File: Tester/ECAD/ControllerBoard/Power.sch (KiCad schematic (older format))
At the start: 10 parts, among them U6 TPS2041B, U7 TLV70033_SOT23-5, U8 TLV70033_SOT23-5

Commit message: Progressed circuit layout.
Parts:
- removed U6: TPS2041B, Package_TO_SOT_SMD:SOT-23-5, symbol Power_Management:TPS2041B
- added C10: 0.1uC, Capacitor_SMD:C_0805_2012Metric_Pad1.15x1.40mm_HandSolder, symbol Device:C
- added C11: 150uCP, symbol Device:CP
- added R23: 10kR, Resistor_SMD:R_0805_2012Metric_Pad1.15x1.40mm_HandSolder, symbol Device:R
- added U6: TPS2046B, Package_SO:SOIC-8_3.9x4.9mm_P1.27mm, symbol Power_Management_Custom:TPS2046B
- R6: value R -> 10kR
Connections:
- net labels added: LOAD_OVERCURRENT_DIGITAL_LOGIC, LOAD_OVERCURRENT_MOTOR, V3_3, ~POWER_SWITCH_ANALOGUE_LOADS, ~POWER_SWITCH_DIGITAL_LOGIC
- net labels removed: V3_3_SENS, ~POWER_SWITCH
- wire segments 49 -> 71
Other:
- moved on the sheet: C31, C32, C8, C9, R6, U8

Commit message: Update Power.sch
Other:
- moved on the sheet: C8
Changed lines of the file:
@@
 L Device:C C8
 U 1 1 5E61FCAC
-P 7000 2250
-F 0 "C8" H 7115 2296 50  0000 L CNN
-F 1 "0.1uC" H 7115 2205 50  0000 L CNN
-F 2 "Capacitor_SMD:C_0805_2012Metric_Pad1.15x1.40mm_HandSolder" H 7038 2100 50  0001 C CNN
-F 3 "~" H 7000 2250 50  0001 C CNN
-F 4 "" H 7000 2250 50  0001 C CNN "Manufacturer Part Number"
-	1    7000 2250
+P 6700 3150
+F 0 "C8" H 6815 3196 50  0000 L CNN
+F 1 "0.1uC" H 6815 3105 50  0000 L CNN
+F 2 "Capacitor_SMD:C_0805_2012Metric_Pad1.15x1.40mm_HandSolder" H 6738 3000 50  0001 C CNN
+F 3 "~" H 6700 3150 50  0001 C CNN
+F 4 "" H 6700 3150 50  0001 C CNN "Manufacturer Part Number"
+	1    6700 3150
 	1    0    0    -1
 $EndComp
-Wire Wire Line
-	6700 2000 7000 2000
-Connection ~ 6700 2000
 Connection ~ 6000 3650
 $Comp
@@
 Text HLabel 4750 2700 0    50   Output ~ 0
 LOAD_OVERCURRENT_DIGITAL_LOGIC
-Wire Wire Line
-	7000 2100 7000 2000
-Wire Wire Line
-	7000 2400 7000 3650
-Wire Wire Line
-	7000 3650 6000 3650
 Connection ~ 7200 2800
 Wire Wire Line
 	7200 3300 7200 3650
-Wire Wire Line
-	7200 3650 7000 3650
-Connection ~ 7000 3650
 $Comp
 L Device:C C10
@@
 Wire Wire Line
 	7750 2800 9100 2800
+Connection ~ 6700 2600
+Connection ~ 6700 3650
+Wire Wire Line
+	6700 3650 6000 3650
+Wire Wire Line
+	6700 3650 7200 3650
+Wire Wire Line
+	6700 3000 6700 2600
+Wire Wire Line
+	6700 3300 6700 3650
 $EndSCHEMATC

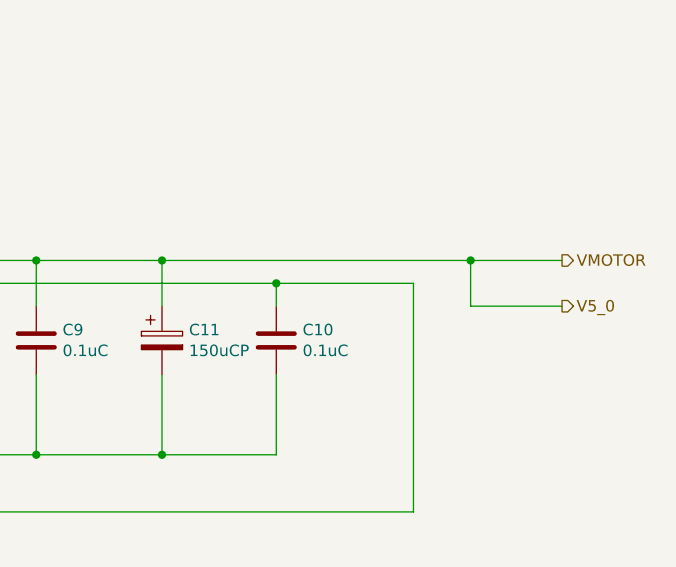
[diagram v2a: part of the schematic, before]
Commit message: Progressed circuit layout.
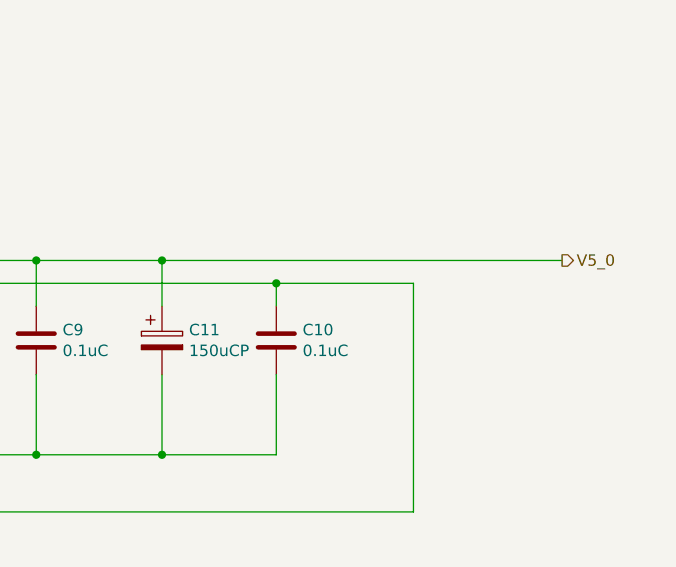
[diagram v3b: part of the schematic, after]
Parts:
- C10, C8, C9: Manufacturer Part Number (none) -> CC0805ZRY5V8BB104
- C11: footprint (none) -> Capacitor_Tantalum_SMD:CP_EIA-7343-31_Kemet-D_Pad2.25x2.55mm_HandSolder
- R23, R6: Manufacturer Part Number (none) -> RC0805FR-0710KL
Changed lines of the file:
@@
 Text HLabel 850  7500 0    50   Input ~ 0
 GND
-Text HLabel 9500 2800 2    50   Output ~ 0
-VMOTOR
 Text HLabel 9400 1050 2    50   Output ~ 0
 V3_3_MCU
-Text HLabel 9500 3000 2    50   Output ~ 0
+Text HLabel 9500 2800 2    50   Output ~ 0
 V5_0
 $Comp
@@
 F 2 "Capacitor_SMD:C_0805_2012Metric_Pad1.15x1.40mm_HandSolder" H 6738 3000 50  0001 C CNN
 F 3 "~" H 6700 3150 50  0001 C CNN
-F 4 "" H 6700 3150 50  0001 C CNN "Manufacturer Part Number"
+F 4 "CC0805ZRY5V8BB104" H 6700 3150 50  0001 C CNN "Manufacturer Part Number"
 	1    6700 3150
 	1    0    0    -1
@@
 F 2 "Capacitor_SMD:C_0805_2012Metric_Pad1.15x1.40mm_HandSolder" H 7238 3000 50  0001 C CNN
 F 3 "~" H 7200 3150 50  0001 C CNN
-F 4 "" H 7200 3150 50  0001 C CNN "Manufacturer Part Number"
+F 4 "CC0805ZRY5V8BB104" H 7200 3150 50  0001 C CNN "Manufacturer Part Number"
 	1    7200 3150
 	1    0    0    -1
@@
 F 2 "Resistor_SMD:R_0805_2012Metric_Pad1.15x1.40mm_HandSolder" V 4780 2300 50  0001 C CNN
 F 3 "~" H 4850 2300 50  0001 C CNN
+F 4 "RC0805FR-0710KL" H 4850 2300 50  0001 C CNN "Manufacturer Part Number"
 	1    4850 2300
 	1    0    0    -1
@@
 Wire Wire Line
 	4950 3900 4950 4350
-Wire Wire Line
-	9500 3000 9100 3000
-Wire Wire Line
-	9100 3000 9100 2800
-Connection ~ 9100 2800
-Wire Wire Line
-	9100 2800 9500 2800
 Text HLabel 5500 3100 0    50   Input ~ 0
 ~POWER_SWITCH_DIGITAL_LOGIC
@@
 F 2 "Resistor_SMD:R_0805_2012Metric_Pad1.15x1.40mm_HandSolder" V 5130 2300 50  0001 C CNN
 F 3 "~" H 5200 2300 50  0001 C CNN
+F 4 "RC0805FR-0710KL" H 5200 2300 50  0001 C CNN "Manufacturer Part Number"
 	1    5200 2300
 	1    0    0    -1
@@
 F 2 "Capacitor_SMD:C_0805_2012Metric_Pad1.15x1.40mm_HandSolder" H 8288 3000 50  0001 C CNN
 F 3 "~" H 8250 3150 50  0001 C CNN
-F 4 "" H 8250 3150 50  0001 C CNN "Manufacturer Part Number"
+F 4 "CC0805ZRY5V8BB104" H 8250 3150 50  0001 C CNN "Manufacturer Part Number"
 	1    8250 3150
 	1    0    0    -1
@@
 F 0 "C11" H 7868 3196 50  0000 L CNN
 F 1 "150uCP" H 7868 3105 50  0000 L CNN
-F 2 "" H 7788 3000 50  0001 C CNN
+F 2 "Capacitor_Tantalum_SMD:CP_EIA-7343-31_Kemet-D_Pad2.25x2.55mm_HandSolder" H 7788 3000 50  0001 C CNN
 F 3 "~" H 7750 3150 50  0001 C CNN
 F 4 "T495D157K010ATE100" H 7750 3150 50  0001 C CNN "Manufacturer Part Number"
@@
 	7750 3000 7750 2800
 Connection ~ 7750 2800
-Wire Wire Line
-	7750 2800 9100 2800
 Connection ~ 6700 2600
 Connection ~ 6700 3650
@@
 Wire Wire Line
 	6700 3300 6700 3650
+Wire Wire Line
+	7750 2800 9500 2800
 $EndSCHEMATC

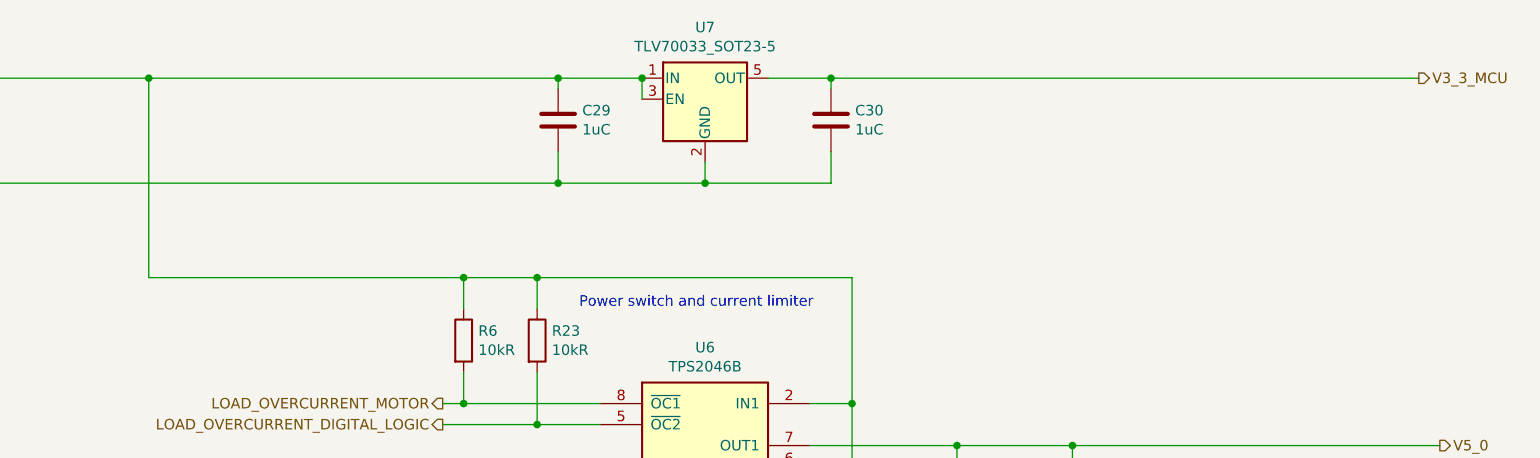
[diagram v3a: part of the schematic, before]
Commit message: Progressed circuit layout.
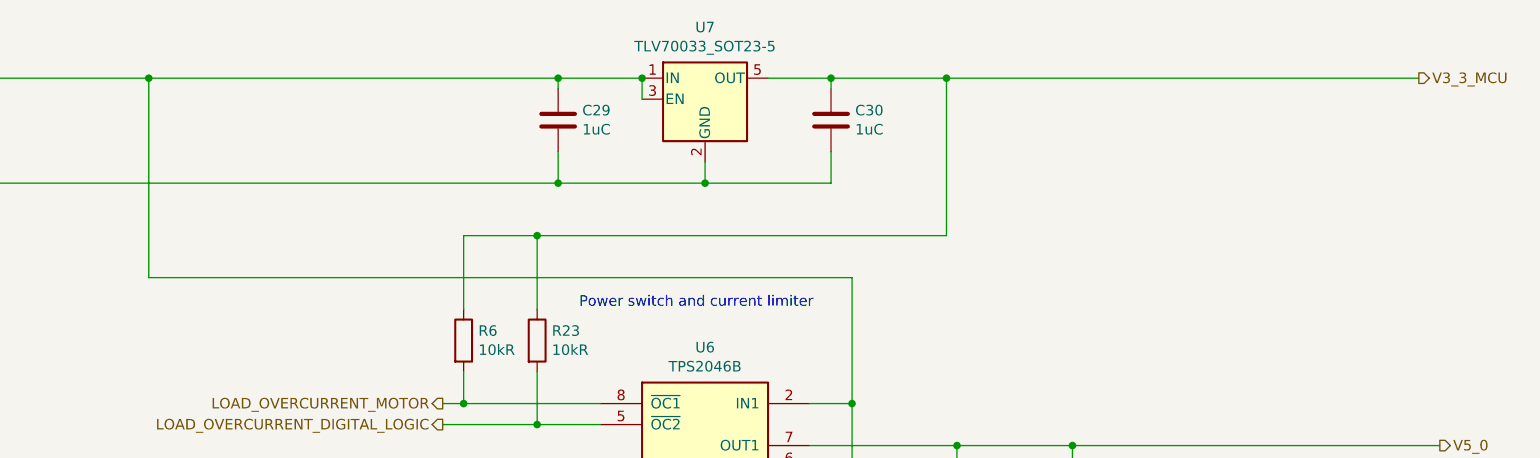
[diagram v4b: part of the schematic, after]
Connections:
- net V3_3_MCU: now also R23.1, R6.1
- net V5_USB: no longer R23.1, R6.1
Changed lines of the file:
@@
 Connection ~ 6600 1050
 Wire Wire Line
-	6600 1050 9400 1050
+	6600 1050 7150 1050
 Wire Wire Line
 	6600 1400 6600 1550
@@
 	6500 2600 6700 2600
 Wire Wire Line
-	6700 2000 5200 2000
-Wire Wire Line
 	3350 2000 3350 1050
 Connection ~ 3350 1050
@@
 Wire Wire Line
 	4850 2600 4850 2450
-Wire Wire Line
-	4850 2150 4850 2000
 Text Notes 5400 2150 0    50   ~ 0
 Power switch and current limiter
@@
 	5200 2700 5200 2450
 Wire Wire Line
-	5200 2150 5200 2000
-Connection ~ 5200 2000
-Wire Wire Line
 	5200 2700 4750 2700
 Connection ~ 5200 2700
@@
 	7750 3650 7200 3650
 Connection ~ 7200 3650
-Connection ~ 4850 2000
-Wire Wire Line
-	4850 2000 3350 2000
-Wire Wire Line
-	4850 2000 5200 2000
 Connection ~ 4850 2600
 Wire Wire Line
@@
 Wire Wire Line
 	7750 2800 9500 2800
+Wire Wire Line
+	3350 2000 6700 2000
+Wire Wire Line
+	7150 1050 7150 1800
+Wire Wire Line
+	7150 1800 5200 1800
+Wire Wire Line
+	4850 1800 4850 2150
+Connection ~ 7150 1050
+Wire Wire Line
+	7150 1050 9400 1050
+Wire Wire Line
+	5200 2150 5200 1800
+Connection ~ 5200 1800
+Wire Wire Line
+	5200 1800 4850 1800
 $EndSCHEMATC

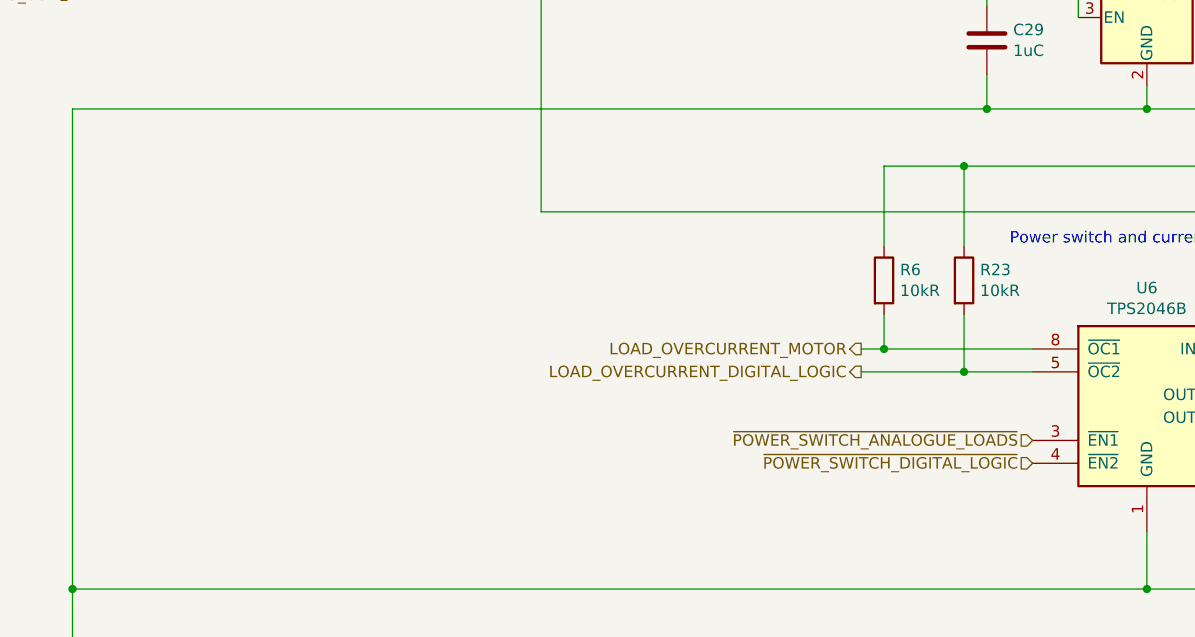
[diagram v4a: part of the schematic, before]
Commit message: Progressed circuit layout.
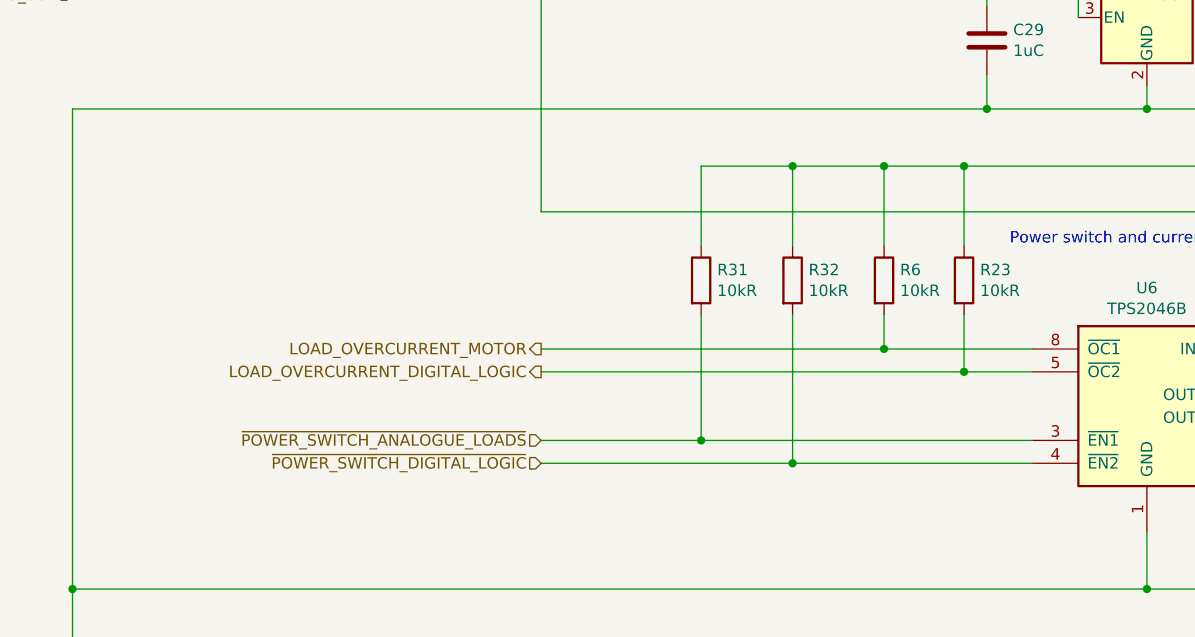
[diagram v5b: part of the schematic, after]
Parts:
- added R31, R32: 10kR, Resistor_SMD:R_0805_2012Metric_Pad1.15x1.40mm_HandSolder, symbol Device:R
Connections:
- net V3_3_MCU: now also R31.1, R32.1
- net ~POWER_SWITCH_ANALOGUE_LOADS: now also R31.2
- net ~POWER_SWITCH_DIGITAL_LOGIC: now also R32.2
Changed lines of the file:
@@
 Wire Wire Line
 	7200 2800 7200 3000
-Text HLabel 5500 3000 0    50   Input ~ 0
+Text HLabel 3350 3000 0    50   Input ~ 0
 ~POWER_SWITCH_ANALOGUE_LOADS
 $Comp
@@
 Text Notes 5400 2150 0    50   ~ 0
 Power switch and current limiter
-Text HLabel 4750 2600 0    50   Output ~ 0
+Text HLabel 3350 2600 0    50   Output ~ 0
 LOAD_OVERCURRENT_MOTOR
 Wire Wire Line
@@
 Wire Wire Line
 	4950 3900 4950 4350
-Text HLabel 5500 3100 0    50   Input ~ 0
+Text HLabel 3350 3100 0    50   Input ~ 0
 ~POWER_SWITCH_DIGITAL_LOGIC
 $Comp
@@
 Wire Wire Line
 	5200 2700 5200 2450
-Wire Wire Line
-	5200 2700 4750 2700
 Connection ~ 5200 2700
-Text HLabel 4750 2700 0    50   Output ~ 0
+Text HLabel 3350 2700 0    50   Output ~ 0
 LOAD_OVERCURRENT_DIGITAL_LOGIC
 Connection ~ 7200 2800
@@
 Connection ~ 4850 2600
 Wire Wire Line
-	4850 2600 4750 2600
-Wire Wire Line
 	4850 2600 5500 2600
 $Comp
@@
 Wire Wire Line
 	5200 1800 4850 1800
+$Comp
+L Device:R R31
+U 1 1 5E6464A0
+P 4050 2300
+F 0 "R31" H 4120 2346 50  0000 L CNN
+F 1 "10kR" H 4120 2255 50  0000 L CNN
+F 2 "Resistor_SMD:R_0805_2012Metric_Pad1.15x1.40mm_HandSolder" V 3980 2300 50  0001 C CNN
+F 3 "~" H 4050 2300 50  0001 C CNN
+F 4 "RC0805FR-0710KL" H 4050 2300 50  0001 C CNN "Manufacturer Part Number"
+	1    4050 2300
+	1    0    0    -1
+$EndComp
+$Comp
+L Device:R R32
+U 1 1 5E64669F
+P 4450 2300
+F 0 "R32" H 4520 2346 50  0000 L CNN
+F 1 "10kR" H 4520 2255 50  0000 L CNN
+F 2 "Resistor_SMD:R_0805_2012Metric_Pad1.15x1.40mm_HandSolder" V 4380 2300 50  0001 C CNN
+F 3 "~" H 4450 2300 50  0001 C CNN
+F 4 "RC0805FR-0710KL" H 4450 2300 50  0001 C CNN "Manufacturer Part Number"
+	1    4450 2300
+	1    0    0    -1
+$EndComp
+Wire Wire Line
+	3350 2600 4850 2600
+Wire Wire Line
+	3350 2700 5200 2700
+Wire Wire Line
+	5500 3000 4050 3000
+Wire Wire Line
+	5500 3100 4450 3100
+Wire Wire Line
+	4450 2450 4450 3100
+Connection ~ 4450 3100
+Wire Wire Line
+	4450 3100 3350 3100
+Wire Wire Line
+	4050 2450 4050 3000
+Connection ~ 4050 3000
+Wire Wire Line
+	4050 3000 3350 3000
+Wire Wire Line
+	4050 2150 4050 1800
+Wire Wire Line
+	4050 1800 4450 1800
+Connection ~ 4850 1800
+Wire Wire Line
+	4450 2150 4450 1800
+Connection ~ 4450 1800
+Wire Wire Line
+	4450 1800 4850 1800
 $EndSCHEMATC

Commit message: Progressed PCB layout.
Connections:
- net OUT2: now reaches C10.1, C31.1, U6.6 (OUT2), U8.1 (IN), U8.3 (EN)
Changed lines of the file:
@@
 Wire Wire Line
 	4450 1800 4850 1800
+Text Label 6900 3900 0    50   ~ 0
+OUT2
 $EndSCHEMATC

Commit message: Progressed circuit updates.
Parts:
- removed C31, C32: 1uC, Capacitor_SMD:C_0805_2012Metric_Pad1.15x1.40mm_HandSolder, symbol Device:C
- removed U8: TLV70033_SOT23-5, Package_TO_SOT_SMD:SOT-23-5, symbol Regulator_Linear:TLV70033_SOT23-5
- added NT5: Net-Tie_2, symbol Device:Net-Tie_2
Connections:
- net OUT2 is gone; now on net V5_0: C10.1, U6.6 (OUT2)
- net V5_0: no longer C11.1, C9.1, U6.7 (OUT1)
- net V5_USB: now also NT5.1; no longer C8.1, U6.2 (IN1)
- new net: C8.1, NT5.2, U6.2 (IN1)
- new net V5_0_MOTOR: C11.1, C9.1, U6.7 (OUT1)
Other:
- moved on the sheet: C10, C11, C29, C30, C8, C9, R23, R31, R32, R6, U6, U7
